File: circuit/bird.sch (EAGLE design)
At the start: 9 parts, among them U1 ATTINY84-20SSU

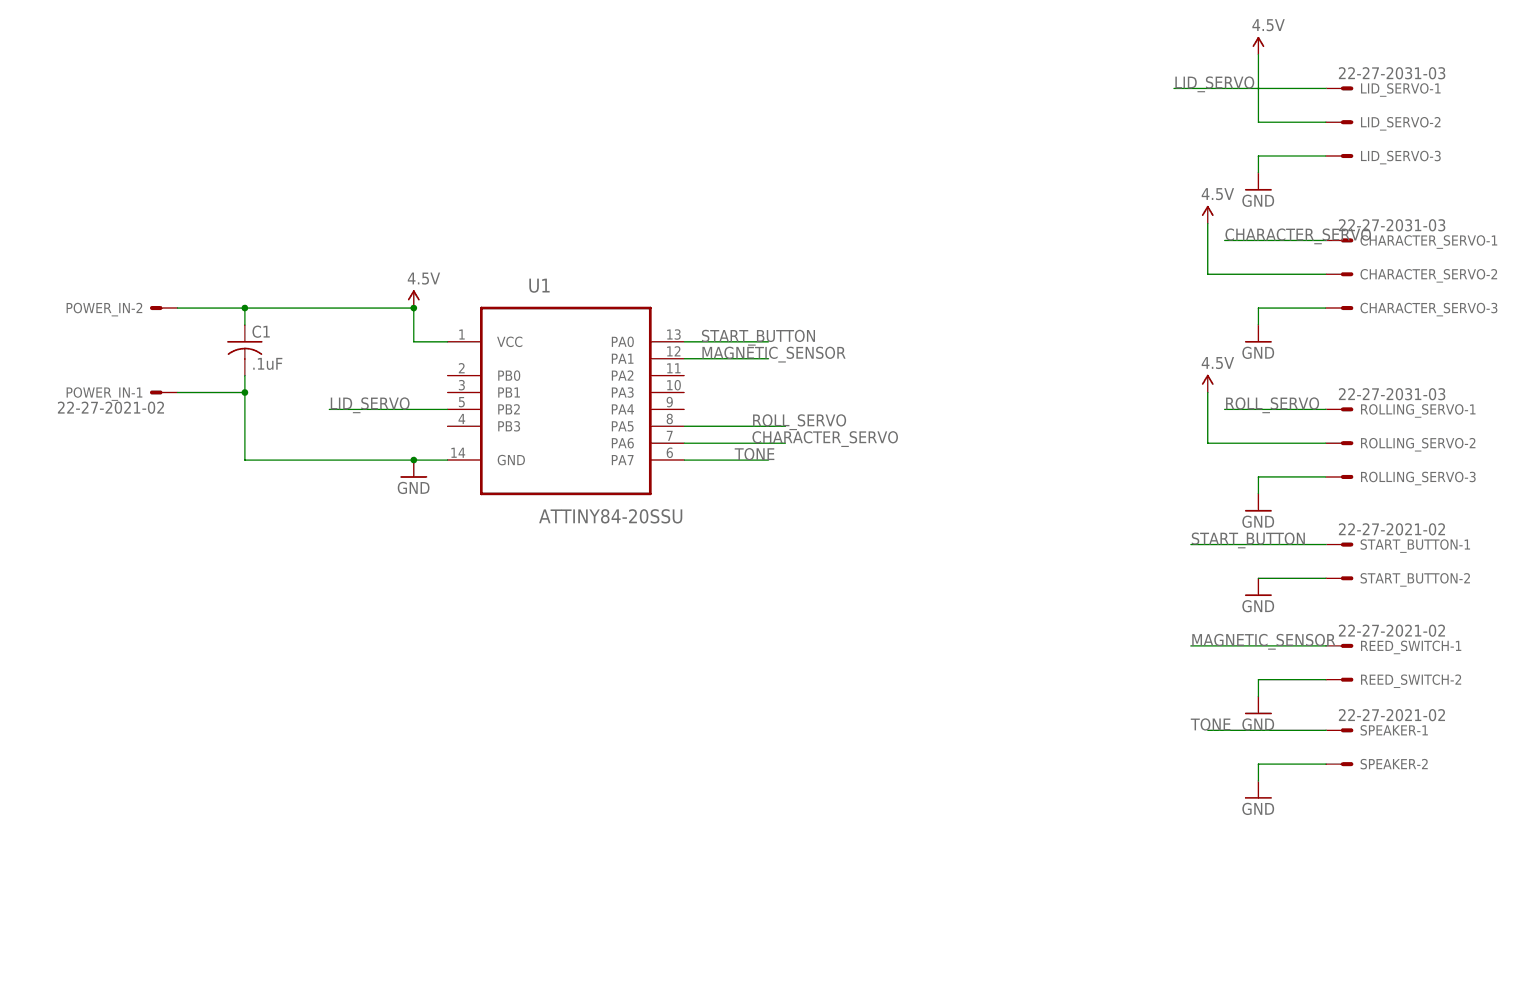
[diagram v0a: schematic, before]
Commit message: update circuit to add programming header
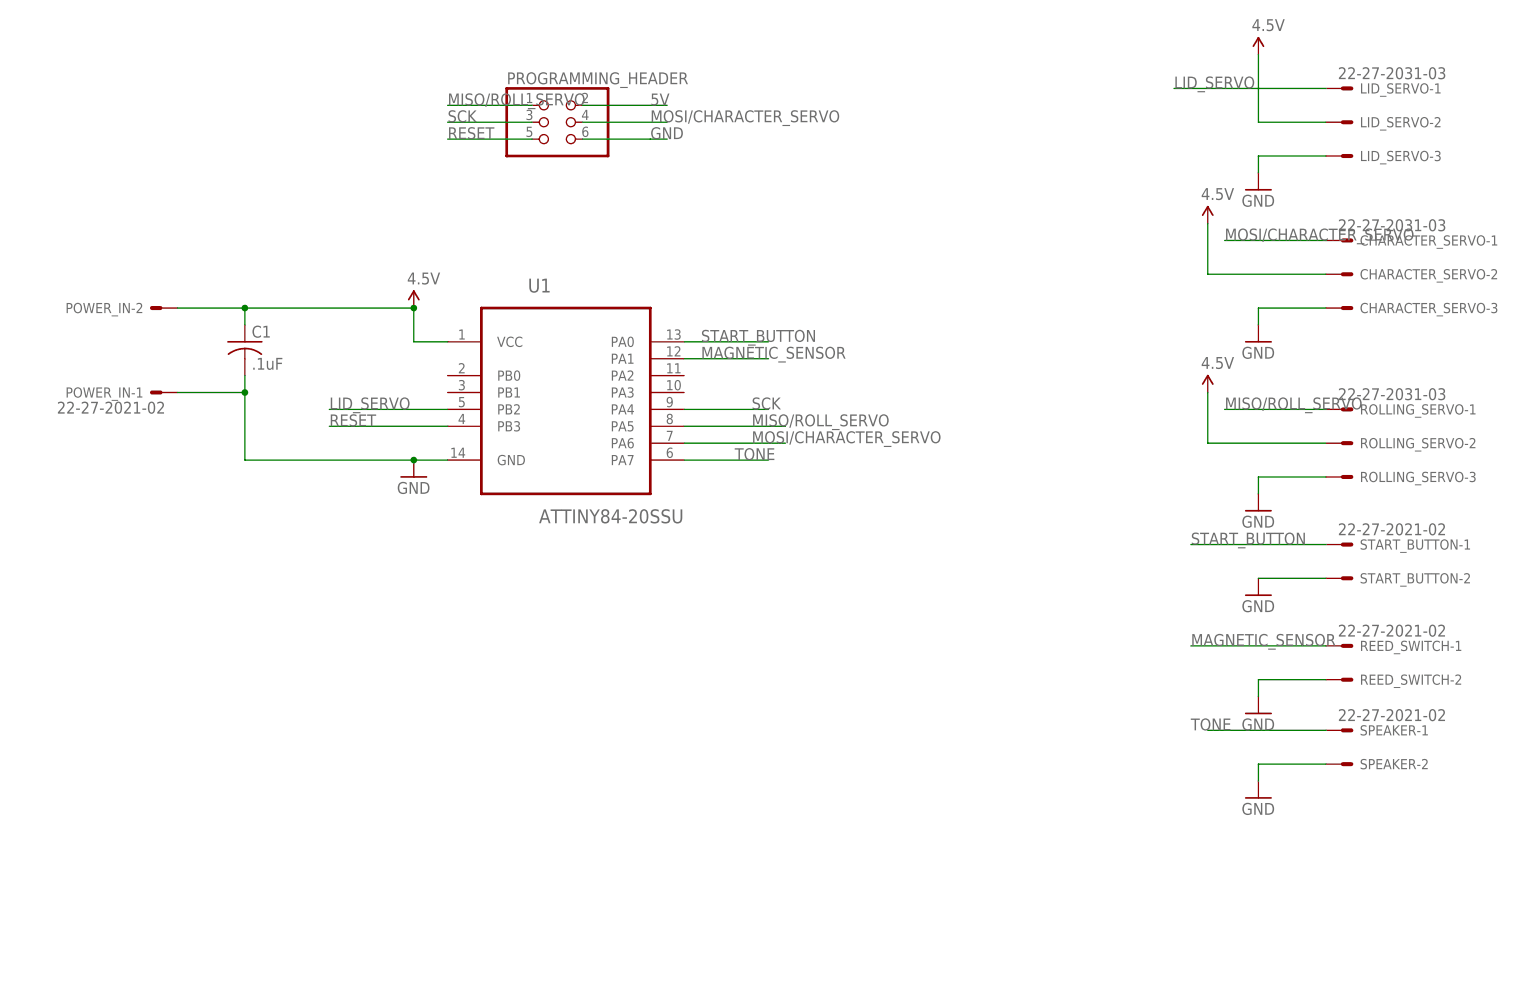
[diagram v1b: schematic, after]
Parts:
- added PROGRAMMING_HEADER: (no value), pinhead:PINHD-2X3
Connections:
- removed net CHARACTER_SERVO: CHARACTER_SERVO-1.S, U1.PA6
- removed net ROLL_SERVO: ROLLING_SERVO-1.S, U1.PA5
- new net MISO/ROLL_SERVO: PROGRAMMING_HEADER.1, ROLLING_SERVO-1.S, U1.PA5
- new net MOSI/CHARACTER_SERVO: CHARACTER_SERVO-1.S, PROGRAMMING_HEADER.4, U1.PA6
- new net RESET: PROGRAMMING_HEADER.5, U1.PB3
- new net SCK: PROGRAMMING_HEADER.3, U1.PA4
- net 5V: now also PROGRAMMING_HEADER.2
- net GND: now also PROGRAMMING_HEADER.6
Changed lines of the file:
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@@
 <part name="U$3" library="SparkFun" deviceset="5V" device="" value="4.5V"/>
 <part name="U$4" library="SparkFun" deviceset="5V" device="" value="4.5V"/>
+<part name="PROGRAMMING_HEADER" library="pinhead" deviceset="PINHD-2X3" device=""/>
 </parts>
 <sheets>
@@
 <instance part="U$3" gate="G$1" x="99.06" y="66.04"/>
 <instance part="U$4" gate="G$1" x="99.06" y="40.64"/>
+<instance part="PROGRAMMING_HEADER" gate="A" x="0" y="81.28"/>
 </instances>
 <busses>
@@
 <wire x1="99.06" y1="58.42" x2="99.06" y2="66.04" width="0.1524" layer="91"/>
 </segment>
+<segment>
+<pinref part="PROGRAMMING_HEADER" gate="A" pin="2"/>
+<wire x1="5.08" y1="83.82" x2="17.78" y2="83.82" width="0.1524" layer="91"/>
+<label x="15.24" y="83.82" size="1.778" layer="95"/>
+</segment>
 </net>
 <net name="GND" class="0">
@@
 <wire x1="106.68" y1="76.2" x2="106.68" y2="73.66" width="0.1524" layer="91"/>
 </segment>
+<segment>
+<pinref part="PROGRAMMING_HEADER" gate="A" pin="6"/>
+<wire x1="5.08" y1="78.74" x2="15.24" y2="78.74" width="0.1524" layer="91"/>
+<wire x1="15.24" y1="78.74" x2="17.78" y2="78.74" width="0.1524" layer="91"/>
+<label x="15.24" y="78.74" size="1.778" layer="95"/>
+</segment>
 </net>
 <net name="TONE" class="0">
@@
 </segment>
 </net>
-<net name="ROLL_SERVO" class="0">
+<net name="MISO/ROLL_SERVO" class="0">
 <segment>
 <pinref part="ROLLING_SERVO" gate="-1" pin="S"/>
@@
 <label x="30.48" y="35.56" size="1.778" layer="95"/>
 </segment>
-</net>
-<net name="CHARACTER_SERVO" class="0">
+<segment>
+<pinref part="PROGRAMMING_HEADER" gate="A" pin="1"/>
+<wire x1="-2.54" y1="83.82" x2="-15.24" y2="83.82" width="0.1524" layer="91"/>
+<label x="-15.24" y="83.82" size="1.778" layer="95"/>
+</segment>
+</net>
+<net name="MOSI/CHARACTER_SERVO" class="0">
 <segment>
 <pinref part="CHARACTER_SERVO" gate="-1" pin="S"/>
@@
 <label x="30.48" y="33.02" size="1.778" layer="95"/>
 </segment>
+<segment>
+<pinref part="PROGRAMMING_HEADER" gate="A" pin="4"/>
+<wire x1="5.08" y1="81.28" x2="17.78" y2="81.28" width="0.1524" layer="91"/>
+<label x="15.24" y="81.28" size="1.778" layer="95"/>
+</segment>
 </net>
 <net name="LID_SERVO" class="0">
@@
 </segment>
 </net>
+<net name="SCK" class="0">
+<segment>
+<pinref part="PROGRAMMING_HEADER" gate="A" pin="3"/>
+<wire x1="-2.54" y1="81.28" x2="-15.24" y2="81.28" width="0.1524" layer="91"/>
+<label x="-15.24" y="81.28" size="1.778" layer="95"/>
+</segment>
+<segment>
+<pinref part="U1" gate="A" pin="PA4"/>
+<wire x1="20.32" y1="38.1" x2="33.02" y2="38.1" width="0.1524" layer="91"/>
+<label x="30.48" y="38.1" size="1.778" layer="95"/>
+</segment>
+</net>
+<net name="RESET" class="0">
+<segment>
+<pinref part="PROGRAMMING_HEADER" gate="A" pin="5"/>
+<wire x1="-2.54" y1="78.74" x2="-15.24" y2="78.74" width="0.1524" layer="91"/>
+<label x="-15.24" y="78.74" size="1.778" layer="95"/>
+</segment>
+<segment>
+<pinref part="U1" gate="A" pin="PB3"/>
+<wire x1="-15.24" y1="35.56" x2="-33.02" y2="35.56" width="0.1524" layer="91"/>
+<label x="-33.02" y="35.56" size="1.778" layer="95"/>
+</segment>
+</net>

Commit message: add LED
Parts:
- added LED1: red, led:LED5MM
- added R1: 500, rcl:R-US_R1206
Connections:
- new net INDICATOR: LED1.C, U1.PA2
- new net N$1: LED1.A, R1.1
- net 5V: now also R1.2
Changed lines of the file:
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@@
 <grid distance="0.1" unitdist="inch" unit="inch" style="lines" multiple="1" display="no" altdistance="0.01" altunitdist="inch" altunit="inch"/>
 <layers>
-<layer number="1" name="Top" color="4" fill="1" visible="no" active="no"/>
-<layer number="2" name="Route2" color="1" fill="3" visible="no" active="no"/>
-<layer number="3" name="Route3" color="4" fill="3" visible="no" active="no"/>
-<layer number="14" name="Route14" color="1" fill="6" visible="no" active="no"/>
-<layer number="15" name="Route15" color="4" fill="6" visible="no" active="no"/>
-<layer number="16" name="Bottom" color="1" fill="1" visible="no" active="no"/>
-<layer number="17" name="Pads" color="2" fill="1" visible="no" active="no"/>
-<layer number="18" name="Vias" color="2" fill="1" visible="no" active="no"/>
-<layer number="19" name="Unrouted" color="6" fill="1" visible="no" active="no"/>
-<layer number="20" name="Dimension" color="15" fill="1" visible="no" active="no"/>
-<layer number="21" name="tPlace" color="7" fill="1" visible="no" active="no"/>
-<layer number="22" name="bPlace" color="7" fill="1" visible="no" active="no"/>
-<layer number="23" name="tOrigins" color="15" fill="1" visible="no" active="no"/>
-<layer number="24" name="bOrigins" color="15" fill="1" visible="no" active="no"/>
-<layer number="25" name="tNames" color="7" fill="1" visible="no" active="no"/>
-<layer number="26" name="bNames" color="7" fill="1" visible="no" active="no"/>
-<layer number="27" name="tValues" color="7" fill="1" visible="no" active="no"/>
-<layer number="28" name="bValues" color="7" fill="1" visible="no" active="no"/>
+<layer number="1" name="Top" color="4" fill="1" visible="yes" active="no"/>
+<layer number="2" name="Route2" color="1" fill="3" visible="yes" active="no"/>
+<layer number="3" name="Route3" color="4" fill="3" visible="yes" active="no"/>
+<layer number="14" name="Route14" color="1" fill="6" visible="yes" active="no"/>
+<layer number="15" name="Route15" color="4" fill="6" visible="yes" active="no"/>
+<layer number="16" name="Bottom" color="1" fill="1" visible="yes" active="no"/>
+<layer number="17" name="Pads" color="2" fill="1" visible="yes" active="no"/>
+<layer number="18" name="Vias" color="2" fill="1" visible="yes" active="no"/>
+<layer number="19" name="Unrouted" color="6" fill="1" visible="yes" active="no"/>
+<layer number="20" name="Dimension" color="15" fill="1" visible="yes" active="no"/>
+<layer number="21" name="tPlace" color="7" fill="1" visible="yes" active="no"/>
+<layer number="22" name="bPlace" color="7" fill="1" visible="yes" active="no"/>
+<layer number="23" name="tOrigins" color="15" fill="1" visible="yes" active="no"/>
+<layer number="24" name="bOrigins" color="15" fill="1" visible="yes" active="no"/>
+<layer number="25" name="tNames" color="7" fill="1" visible="yes" active="no"/>
+<layer number="26" name="bNames" color="7" fill="1" visible="yes" active="no"/>
+<layer number="27" name="tValues" color="7" fill="1" visible="yes" active="no"/>
+<layer number="28" name="bValues" color="7" fill="1" visible="yes" active="no"/>
 <layer number="29" name="tStop" color="7" fill="3" visible="no" active="no"/>
 <layer number="30" name="bStop" color="7" fill="6" visible="no" active="no"/>
@@
 <layer number="35" name="tGlue" color="7" fill="4" visible="no" active="no"/>
 <layer number="36" name="bGlue" color="7" fill="5" visible="no" active="no"/>
-<layer number="37" name="tTest" color="7" fill="1" visible="no" active="no"/>
-<layer number="38" name="bTest" color="7" fill="1" visible="no" active="no"/>
+<layer number="37" name="tTest" color="7" fill="1" visible="yes" active="no"/>
+<layer number="38" name="bTest" color="7" fill="1" visible="yes" active="no"/>
 <layer number="39" name="tKeepout" color="4" fill="11" visible="no" active="no"/>
 <layer number="40" name="bKeepout" color="1" fill="11" visible="no" active="no"/>
@@
 <layer number="44" name="Drills" color="7" fill="1" visible="no" active="no"/>
 <layer number="45" name="Holes" color="7" fill="1" visible="no" active="no"/>
-<layer number="46" name="Milling" color="3" fill="1" visible="no" active="no"/>
-<layer number="47" name="Measures" color="7" fill="1" visible="no" active="no"/>
-<layer number="48" name="Document" color="7" fill="1" visible="no" active="no"/>
-<layer number="49" name="Reference" color="7" fill="1" visible="no" active="no"/>
-<layer number="50" name="dxf" color="7" fill="1" visible="no" active="no"/>
-<layer number="51" name="tDocu" color="7" fill="1" visible="no" active="no"/>
-<layer number="52" name="bDocu" color="7" fill="1" visible="no" active="no"/>
-<layer number="53" name="tGND_GNDA" color="7" fill="9" visible="no" active="no"/>
-<layer number="54" name="bGND_GNDA" color="1" fill="9" visible="no" active="no"/>
-<layer number="56" name="wert" color="7" fill="1" visible="no" active="no"/>
+<layer number="46" name="Milling" color="3" fill="1" visible="yes" active="no"/>
+<layer number="47" name="Measures" color="7" fill="1" visible="yes" active="no"/>
+<layer number="48" name="Document" color="7" fill="1" visible="yes" active="no"/>
+<layer number="49" name="Reference" color="7" fill="1" visible="yes" active="no"/>
+<layer number="50" name="dxf" color="7" fill="1" visible="yes" active="no"/>
+<layer number="51" name="tDocu" color="7" fill="1" visible="yes" active="no"/>
+<layer number="52" name="bDocu" color="7" fill="1" visible="yes" active="no"/>
+<layer number="53" name="tGND_GNDA" color="7" fill="9" visible="yes" active="no"/>
+<layer number="54" name="bGND_GNDA" color="1" fill="9" visible="yes" active="no"/>
+<layer number="56" name="wert" color="7" fill="1" visible="yes" active="no"/>
 <layer number="91" name="Nets" color="2" fill="1" visible="yes" active="yes"/>
 <layer number="92" name="Busses" color="1" fill="1" visible="yes" active="yes"/>
@@
 <part name="U$4" library="SparkFun" deviceset="5V" device="" value="4.5V"/>
 <part name="PROGRAMMING_HEADER" library="pinhead" deviceset="PINHD-2X3" device=""/>
+<part name="LED1" library="led" deviceset="LED" device="5MM" value="red"/>
+<part name="R1" library="rcl" deviceset="R-US_" device="R1206" value="500"/>
+<part name="P+1" library="supply1" deviceset="+5V" device=""/>
 </parts>
 <sheets>
@@
 <instance part="U$4" gate="G$1" x="99.06" y="40.64"/>
 <instance part="PROGRAMMING_HEADER" gate="A" x="0" y="81.28"/>
+<instance part="LED1" gate="G$1" x="68.58" y="40.64"/>
+<instance part="R1" gate="G$1" x="68.58" y="50.8" rot="R90"/>
+<instance part="P+1" gate="1" x="68.58" y="63.5"/>
 </instances>
 <busses>
@@
 <label x="15.24" y="83.82" size="1.778" layer="95"/>
 </segment>
+<segment>
+<pinref part="R1" gate="G$1" pin="2"/>
+<wire x1="68.58" y1="55.88" x2="68.58" y2="60.96" width="0.1524" layer="91"/>
+<pinref part="P+1" gate="1" pin="+5V"/>
+</segment>
 </net>
 <net name="GND" class="0">
@@
 </segment>
 </net>
+<net name="N$1" class="0">
+<segment>
+<pinref part="R1" gate="G$1" pin="1"/>
+<pinref part="LED1" gate="G$1" pin="A"/>
+<wire x1="68.58" y1="45.72" x2="68.58" y2="43.18" width="0.1524" layer="91"/>
+</segment>
+</net>
+<net name="INDICATOR" class="0">
+<segment>
+<pinref part="LED1" gate="G$1" pin="C"/>
+<wire x1="68.58" y1="35.56" x2="68.58" y2="30.48" width="0.1524" layer="91"/>
+<label x="68.58" y="20.32" size="1.778" layer="95" rot="R90"/>
+</segment>
+<segment>
+<pinref part="U1" gate="A" pin="PA2"/>
+<wire x1="20.32" y1="43.18" x2="35.56" y2="43.18" width="0.1524" layer="91"/>
+<label x="22.86" y="43.18" size="1.778" layer="95"/>
+</segment>
+</net>

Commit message: update circuit
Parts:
- removed REED_SWITCH: 22-27-2021-02, con-molex:22-27-2021-02
- added J1: 22-27-2031-03, con-molex:22-27-2031-03
- added R2, R3: 10k 1%, rcl:R-US_R0603
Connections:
- removed net MISO/ROLL_SERVO: PROGRAMMING_HEADER.1, ROLLING_SERVO-1.S, U1.PA5
- removed net MOSI/CHARACTER_SERVO: CHARACTER_SERVO-1.S, PROGRAMMING_HEADER.4, U1.PA6
- new net CHARACTER_SERVO: CHARACTER_SERVO-1.S, U1.PB1
- new net MAGNETIC_REFERENCE: R2.2, R3.1, U1.PA3
- new net MISO: PROGRAMMING_HEADER.1, U1.PA5
- new net MOSI: PROGRAMMING_HEADER.4, U1.PA6
- new net ROLL_SERVO: ROLLING_SERVO-1.S, U1.PB0
- net 5V: now also J1-1.S, R2.1
- net GND: now also J1-2.S, R3.2; no longer REED_SWITCH-2.S
- net MAGNETIC_SENSOR: now also J1-3.S; no longer REED_SWITCH-1.S
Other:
- moved on the sheet: SPEAKER-1, SPEAKER-2

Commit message: add sensor
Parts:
- removed R2, R3: 10k 1%, rcl:R-US_R0603
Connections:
- removed net MAGNETIC_REFERENCE: R2.2, R3.1, U1.PA3
- net 5V: no longer R2.1
- net GND: no longer R3.2
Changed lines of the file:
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@@
 <part name="R1" library="rcl" deviceset="R-US_" device="R1206" value="500"/>
 <part name="P+1" library="supply1" deviceset="+5V" device=""/>
-<part name="R2" library="rcl" deviceset="R-US_" device="R0603" value="10k 1%"/>
-<part name="R3" library="rcl" deviceset="R-US_" device="R0603" value="10k 1%"/>
-<part name="U$5" library="SparkFun" deviceset="5V" device=""/>
-<part name="GND8" library="SparkFun" deviceset="GND" device=""/>
 <part name="J1" library="con-molex" deviceset="22-?-03" device="27-2031"/>
 <part name="U$6" library="SparkFun" deviceset="5V" device=""/>
@@
 <instance part="R1" gate="G$1" x="68.58" y="50.8" rot="R90"/>
 <instance part="P+1" gate="1" x="68.58" y="63.5"/>
-<instance part="R2" gate="G$1" x="-20.32" y="-10.16"/>
-<instance part="R3" gate="G$1" x="-5.08" y="-10.16"/>
-<instance part="U$5" gate="G$1" x="-30.48" y="-2.54"/>
-<instance part="GND8" gate="1" x="7.62" y="-20.32"/>
 <instance part="J1" gate="-1" x="121.92" y="-5.08"/>
 <instance part="J1" gate="-2" x="121.92" y="-10.16"/>
@@
 </segment>
 <segment>
-<pinref part="R2" gate="G$1" pin="1"/>
-<wire x1="-25.4" y1="-10.16" x2="-30.48" y2="-10.16" width="0.1524" layer="91"/>
-<wire x1="-30.48" y1="-10.16" x2="-30.48" y2="-2.54" width="0.1524" layer="91"/>
-<pinref part="U$5" gate="G$1" pin="5V"/>
-</segment>
-<segment>
 <pinref part="J1" gate="-1" pin="S"/>
 <wire x1="119.38" y1="-5.08" x2="91.44" y2="-5.08" width="0.1524" layer="91"/>
@@
 </segment>
 <segment>
-<pinref part="R3" gate="G$1" pin="2"/>
-<wire x1="0" y1="-10.16" x2="7.62" y2="-10.16" width="0.1524" layer="91"/>
-<wire x1="7.62" y1="-10.16" x2="7.62" y2="-17.78" width="0.1524" layer="91"/>
-<pinref part="GND8" gate="1" pin="GND"/>
-</segment>
-<segment>
 <pinref part="J1" gate="-2" pin="S"/>
 <wire x1="119.38" y1="-10.16" x2="93.98" y2="-10.16" width="0.1524" layer="91"/>
@@
 </segment>
 </net>
-<net name="MAGNETIC_REFERENCE" class="0">
-<segment>
-<pinref part="U1" gate="A" pin="PA3"/>
-<wire x1="20.32" y1="40.64" x2="38.1" y2="40.64" width="0.1524" layer="91"/>
-<label x="22.86" y="40.64" size="1.778" layer="95"/>
-</segment>
-<segment>
-<pinref part="R2" gate="G$1" pin="2"/>
-<pinref part="R3" gate="G$1" pin="1"/>
-<wire x1="-15.24" y1="-10.16" x2="-12.7" y2="-10.16" width="0.1524" layer="91"/>
-<wire x1="-12.7" y1="-10.16" x2="-10.16" y2="-10.16" width="0.1524" layer="91"/>
-<wire x1="-12.7" y1="-10.16" x2="-12.7" y2="2.54" width="0.1524" layer="91"/>
-<junction x="-12.7" y="-10.16"/>
-<wire x1="-12.7" y1="2.54" x2="10.16" y2="2.54" width="0.1524" layer="91"/>
-<label x="-10.16" y="2.54" size="1.778" layer="95"/>
-</segment>
-</net>
